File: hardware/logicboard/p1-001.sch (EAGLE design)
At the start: 36 parts, among them J0 DC9V, J4A RLYOUT-A, J4B RLYOUT-B, J4C RLYOUT-C, J7 DIN5, K1A G5V1, K1B G5V1, K1C G5V1, T1A 2SC1815, T1B 2SC1815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

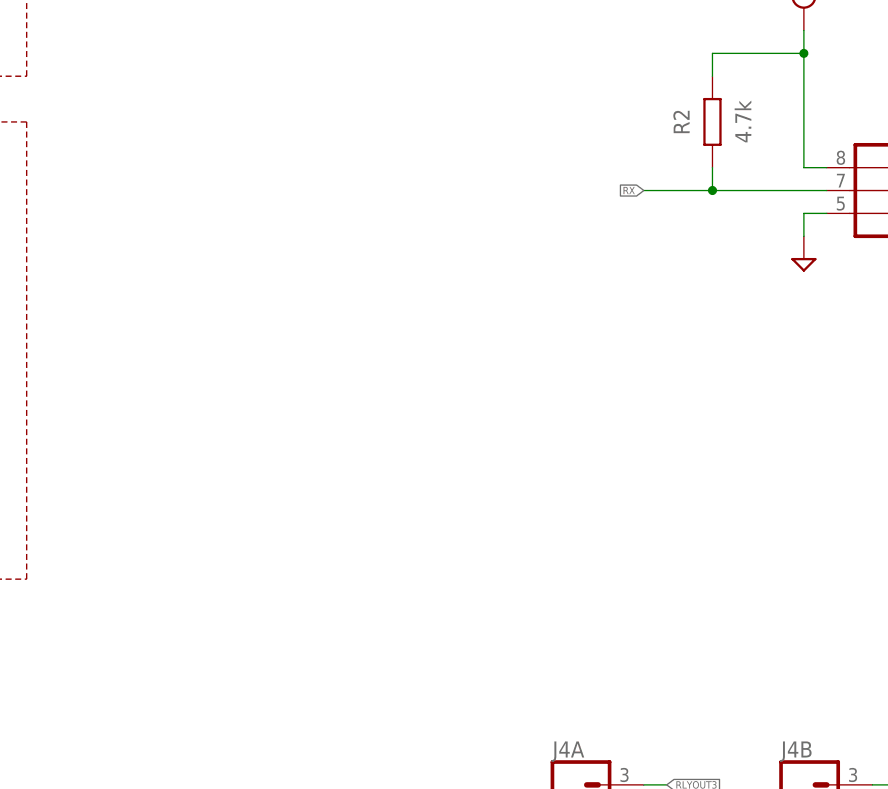
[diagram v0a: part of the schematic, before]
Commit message: J1, J5, and J20.
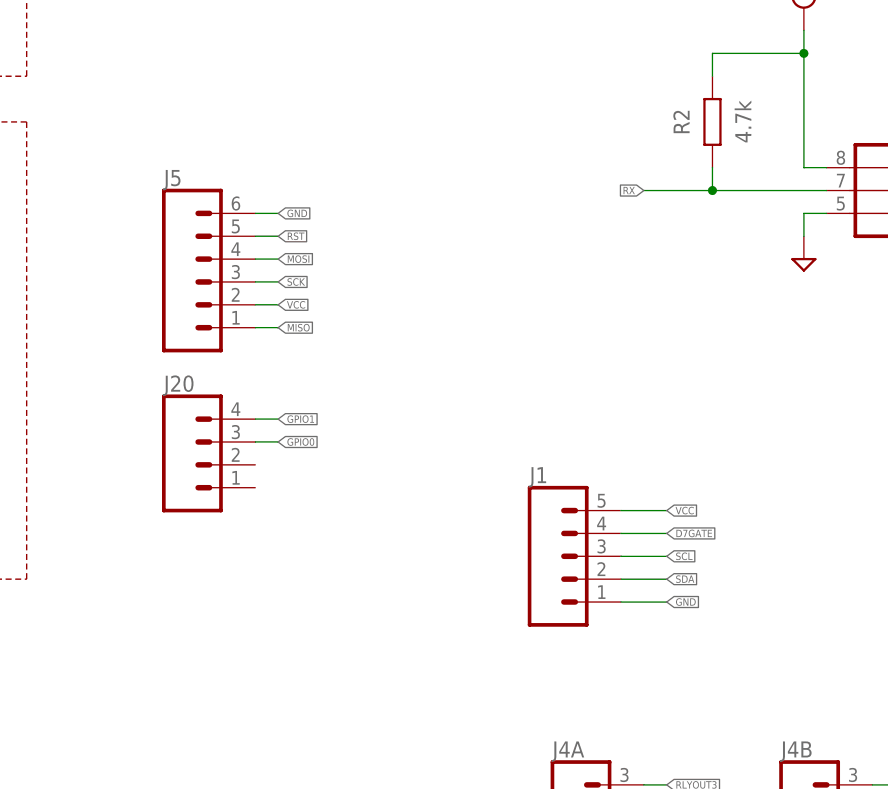
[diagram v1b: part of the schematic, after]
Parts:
- added J1: (no value), SparkFun-Connectors:CONN_05JST
- added J20: (no value), SparkFun-Connectors:CONN_041.27MM
- added J5: (no value), SparkFun-Connectors:CONN_061.27MM
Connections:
- net D7GATE: now also J1.4
- net GND: now also J1.1, J5.6
- net GPIO0: now also J20.3
- net GPIO1: now also J20.4
- net MISO: now also J5.1
- net MOSI: now also J5.4
- net RST: now also J5.5
- net SCK: now also J5.3
- net SCL: now also J1.3
- net SDA: now also J1.2
- net VCC: now also J1.5, J5.2
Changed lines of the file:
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@@
 <part name="J4B" library="SparkFun-Connectors" library_urn="urn:adsk.eagle:library:513" deviceset="CONN_03" device="JST-PTH" package3d_urn="urn:adsk.eagle:package:38069/1" value="RLYOUT-B"/>
 <part name="J4C" library="SparkFun-Connectors" library_urn="urn:adsk.eagle:library:513" deviceset="CONN_03" device="JST-PTH" package3d_urn="urn:adsk.eagle:package:38069/1" value="RLYOUT-C"/>
+<part name="J1" library="SparkFun-Connectors" library_urn="urn:adsk.eagle:library:513" deviceset="CONN_05" device="JST" package3d_urn="urn:adsk.eagle:package:38120/1"/>
+<part name="J5" library="SparkFun-Connectors" library_urn="urn:adsk.eagle:library:513" deviceset="CONN_06" device="1.27MM" package3d_urn="urn:adsk.eagle:package:38131/1"/>
+<part name="J20" library="SparkFun-Connectors" library_urn="urn:adsk.eagle:library:513" deviceset="CONN_04" device="1.27MM" package3d_urn="urn:adsk.eagle:package:38086/1"/>
 </parts>
 <sheets>
@@
 <attribute name="NAME" x="160.02" y="56.388" size="1.778" layer="95" font="vector"/>
 </instance>
+<instance part="J1" gate="G$1" x="109.22" y="78.74" smashed="yes">
+<attribute name="VALUE" x="106.68" y="68.834" size="1.778" layer="96" font="vector"/>
+<attribute name="NAME" x="106.68" y="86.868" size="1.778" layer="95" font="vector"/>
+</instance>
+<instance part="J5" gate="G$1" x="71.12" y="109.22" smashed="yes">
+<attribute name="VALUE" x="66.04" y="99.314" size="1.778" layer="96" font="vector"/>
+<attribute name="NAME" x="66.04" y="119.888" size="1.778" layer="95" font="vector"/>
+</instance>
+<instance part="J20" gate="G$1" x="71.12" y="88.9" smashed="yes">
+<attribute name="VALUE" x="66.04" y="81.534" size="1.778" layer="96" font="vector"/>
+<attribute name="NAME" x="66.04" y="97.028" size="1.778" layer="95" font="vector"/>
+</instance>
 </instances>
 <busses>
@@
 <wire x1="208.28" y1="170.18" x2="200.66" y2="170.18" width="0.1524" layer="91"/>
 <junction x="200.66" y="170.18"/>
+</segment>
+<segment>
+<pinref part="J1" gate="G$1" pin="1"/>
+<wire x1="116.84" y1="73.66" x2="121.92" y2="73.66" width="0.1524" layer="91"/>
+<label x="121.92" y="73.66" size="0.8128" layer="95" xref="yes"/>
+</segment>
+<segment>
+<pinref part="J5" gate="G$1" pin="6"/>
+<wire x1="76.2" y1="116.84" x2="78.74" y2="116.84" width="0.1524" layer="91"/>
+<label x="78.74" y="116.84" size="0.8128" layer="95" xref="yes"/>
 </segment>
 </net>
@@
 <wire x1="200.66" y1="233.68" x2="200.66" y2="208.28" width="0.1524" layer="91"/>
 </segment>
+<segment>
+<pinref part="J1" gate="G$1" pin="5"/>
+<wire x1="116.84" y1="83.82" x2="121.92" y2="83.82" width="0.1524" layer="91"/>
+<label x="121.92" y="83.82" size="0.8128" layer="95" xref="yes"/>
+</segment>
+<segment>
+<pinref part="J5" gate="G$1" pin="2"/>
+<wire x1="76.2" y1="106.68" x2="78.74" y2="106.68" width="0.1524" layer="91"/>
+<label x="78.74" y="106.68" size="0.8128" layer="95" xref="yes"/>
+</segment>
 </net>
 <net name="MIDIINSND" class="0">
@@
 <label x="340.36" y="116.84" size="0.8128" layer="95" rot="MR0" xref="yes"/>
 </segment>
+<segment>
+<pinref part="J5" gate="G$1" pin="5"/>
+<wire x1="76.2" y1="114.3" x2="78.74" y2="114.3" width="0.1524" layer="91"/>
+<label x="78.74" y="114.3" size="0.8128" layer="95" xref="yes"/>
+</segment>
 </net>
 <net name="THS" class="0">
@@
 <label x="317.5" y="195.58" size="0.8128" layer="95" rot="R180" xref="yes"/>
 </segment>
+<segment>
+<pinref part="J1" gate="G$1" pin="2"/>
+<wire x1="116.84" y1="76.2" x2="121.92" y2="76.2" width="0.1524" layer="91"/>
+<label x="121.92" y="76.2" size="0.8128" layer="95" xref="yes"/>
+</segment>
 </net>
 <net name="RLY" class="0">
@@
 <label x="317.5" y="190.5" size="0.8128" layer="95" rot="R180" xref="yes"/>
 </segment>
+<segment>
+<pinref part="J1" gate="G$1" pin="4"/>
+<wire x1="116.84" y1="81.28" x2="121.92" y2="81.28" width="0.1524" layer="91"/>
+<label x="121.92" y="81.28" size="0.8128" layer="95" xref="yes"/>
+</segment>
 </net>
 <net name="GPIO1" class="0">
@@
 <label x="223.52" y="185.42" size="0.8128" layer="95" xref="yes"/>
 </segment>
+<segment>
+<pinref part="J20" gate="G$1" pin="4"/>
+<wire x1="76.2" y1="93.98" x2="78.74" y2="93.98" width="0.1524" layer="91"/>
+<label x="78.74" y="93.98" size="0.8128" layer="95" xref="yes"/>
+</segment>
 </net>
 <net name="GPIO0" class="0">
@@
 <wire x1="157.48" y1="185.42" x2="160.02" y2="185.42" width="0.1524" layer="91"/>
 <label x="160.02" y="185.42" size="0.8128" layer="95" xref="yes"/>
+</segment>
+<segment>
+<pinref part="J20" gate="G$1" pin="3"/>
+<wire x1="76.2" y1="91.44" x2="78.74" y2="91.44" width="0.1524" layer="91"/>
+<label x="78.74" y="91.44" size="0.8128" layer="95" xref="yes"/>
 </segment>
 </net>
@@
 <label x="340.36" y="109.22" size="0.8128" layer="95" rot="R180" xref="yes"/>
 </segment>
+<segment>
+<pinref part="J5" gate="G$1" pin="1"/>
+<wire x1="76.2" y1="104.14" x2="78.74" y2="104.14" width="0.1524" layer="91"/>
+<label x="78.74" y="104.14" size="0.8128" layer="95" xref="yes"/>
+</segment>
 </net>
 <net name="SCK" class="0">
@@
 <label x="340.36" y="106.68" size="0.8128" layer="95" rot="R180" xref="yes"/>
 </segment>
+<segment>
+<pinref part="J5" gate="G$1" pin="3"/>
+<wire x1="76.2" y1="109.22" x2="78.74" y2="109.22" width="0.1524" layer="91"/>
+<label x="78.74" y="109.22" size="0.8128" layer="95" xref="yes"/>
+</segment>
 </net>
 <net name="MOSI" class="0">
@@
 <label x="370.84" y="106.68" size="0.8128" layer="95" xref="yes"/>
 </segment>
+<segment>
+<pinref part="J5" gate="G$1" pin="4"/>
+<wire x1="76.2" y1="111.76" x2="78.74" y2="111.76" width="0.1524" layer="91"/>
+<label x="78.74" y="111.76" size="0.8128" layer="95" xref="yes"/>
+</segment>
 </net>
 <net name="SCL" class="0">
@@
 <label x="317.5" y="193.04" size="0.8128" layer="95" rot="R180" xref="yes"/>
 </segment>
-</net>
+<segment>
+<pinref part="J1" gate="G$1" pin="3"/>
+<wire x1="116.84" y1="78.74" x2="121.92" y2="78.74" width="0.1524" layer="91"/>
+<label x="121.92" y="78.74" size="0.8128" layer="95" xref="yes"/>
+</segment>
+</net>
